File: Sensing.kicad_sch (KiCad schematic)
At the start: 20 parts

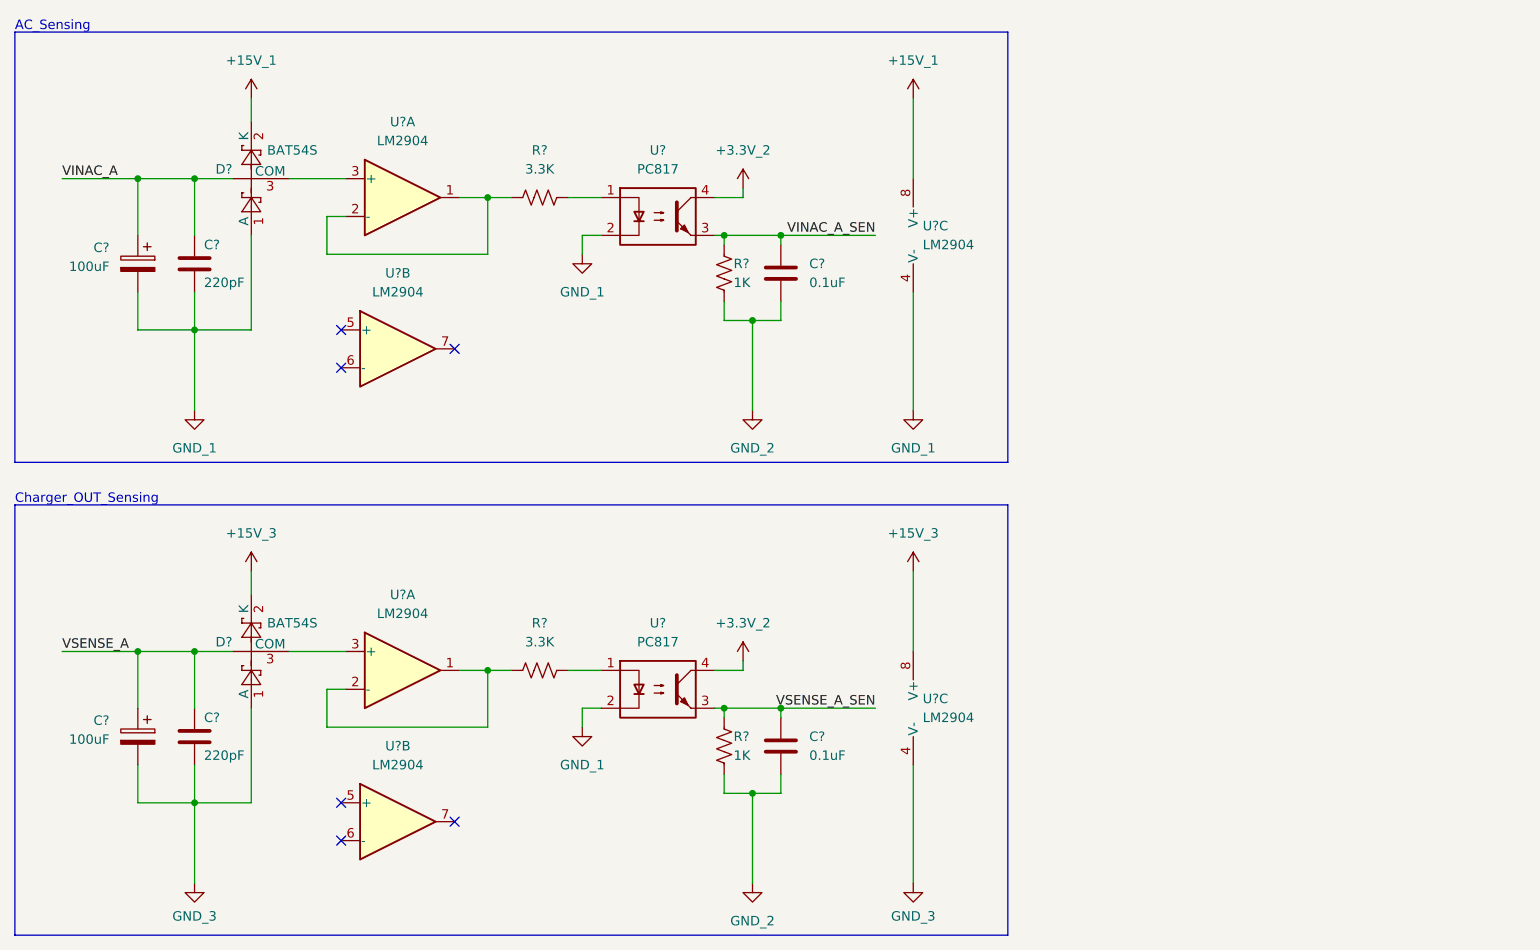
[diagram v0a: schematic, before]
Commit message: Current Sensing added
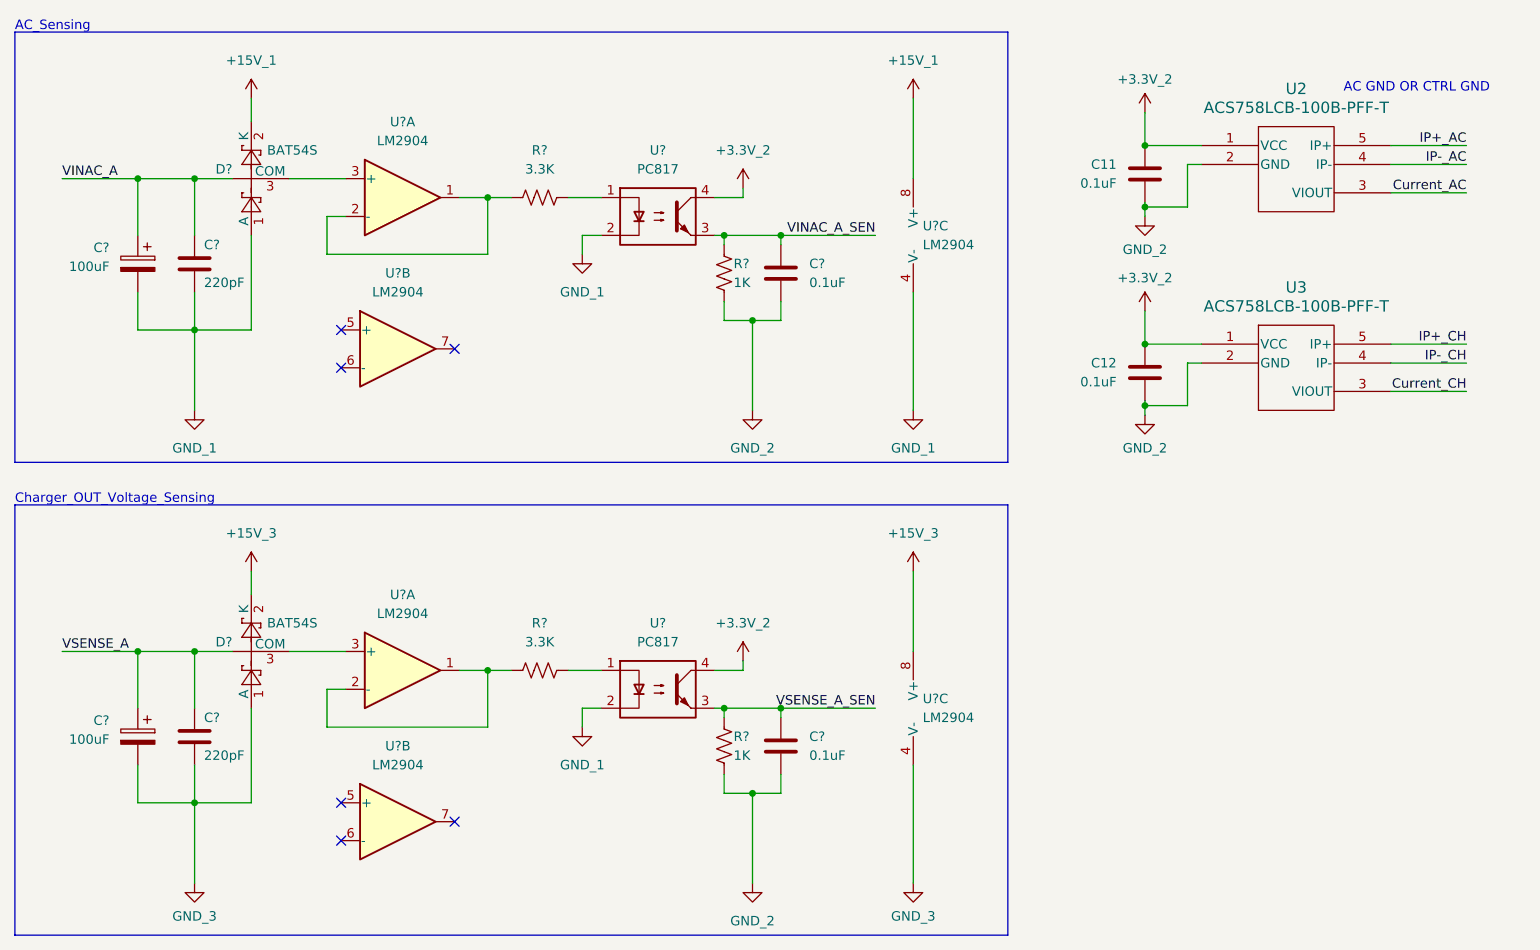
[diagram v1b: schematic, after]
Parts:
- added C11, C12: 0.1uF, Capacitor_SMD:C_0603_1608Metric, symbol Major_Project:0.1uF
- added U2, U3: ACS758LCB-100B-PFF-T, Major_Project:PFF-5_ALM, symbol Major_Project:ACS758LCB-100B-PFF-T
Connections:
- net +3.3V_2: now also C11.1, C12.1, U2.1 (VCC), U3.1 (VCC)
- net GND_2: now also C11.2, C12.2, U2.2 (GND), U3.2 (GND)
- new net Current_AC: U2.3 (VIOUT)
- new net Current_CH: U3.3 (VIOUT)
- new net IP+_AC: U2.5 (IP+)
- new net IP+_CH: U3.5 (IP+)
- new net IP-_AC: U2.4 (IP-)
- new net IP-_CH: U3.4 (IP-)
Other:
- note added: "AC GND OR CTRL GND"
- note added: "Charger_OUT_Voltage_Sensing"
- note removed: "Charger_OUT_Sensing"
